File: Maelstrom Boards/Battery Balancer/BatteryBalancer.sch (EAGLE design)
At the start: 34 parts, among them P2 39-30-16, Q1 SPB80P06P, Q4 310mA/60V/1.6Ω

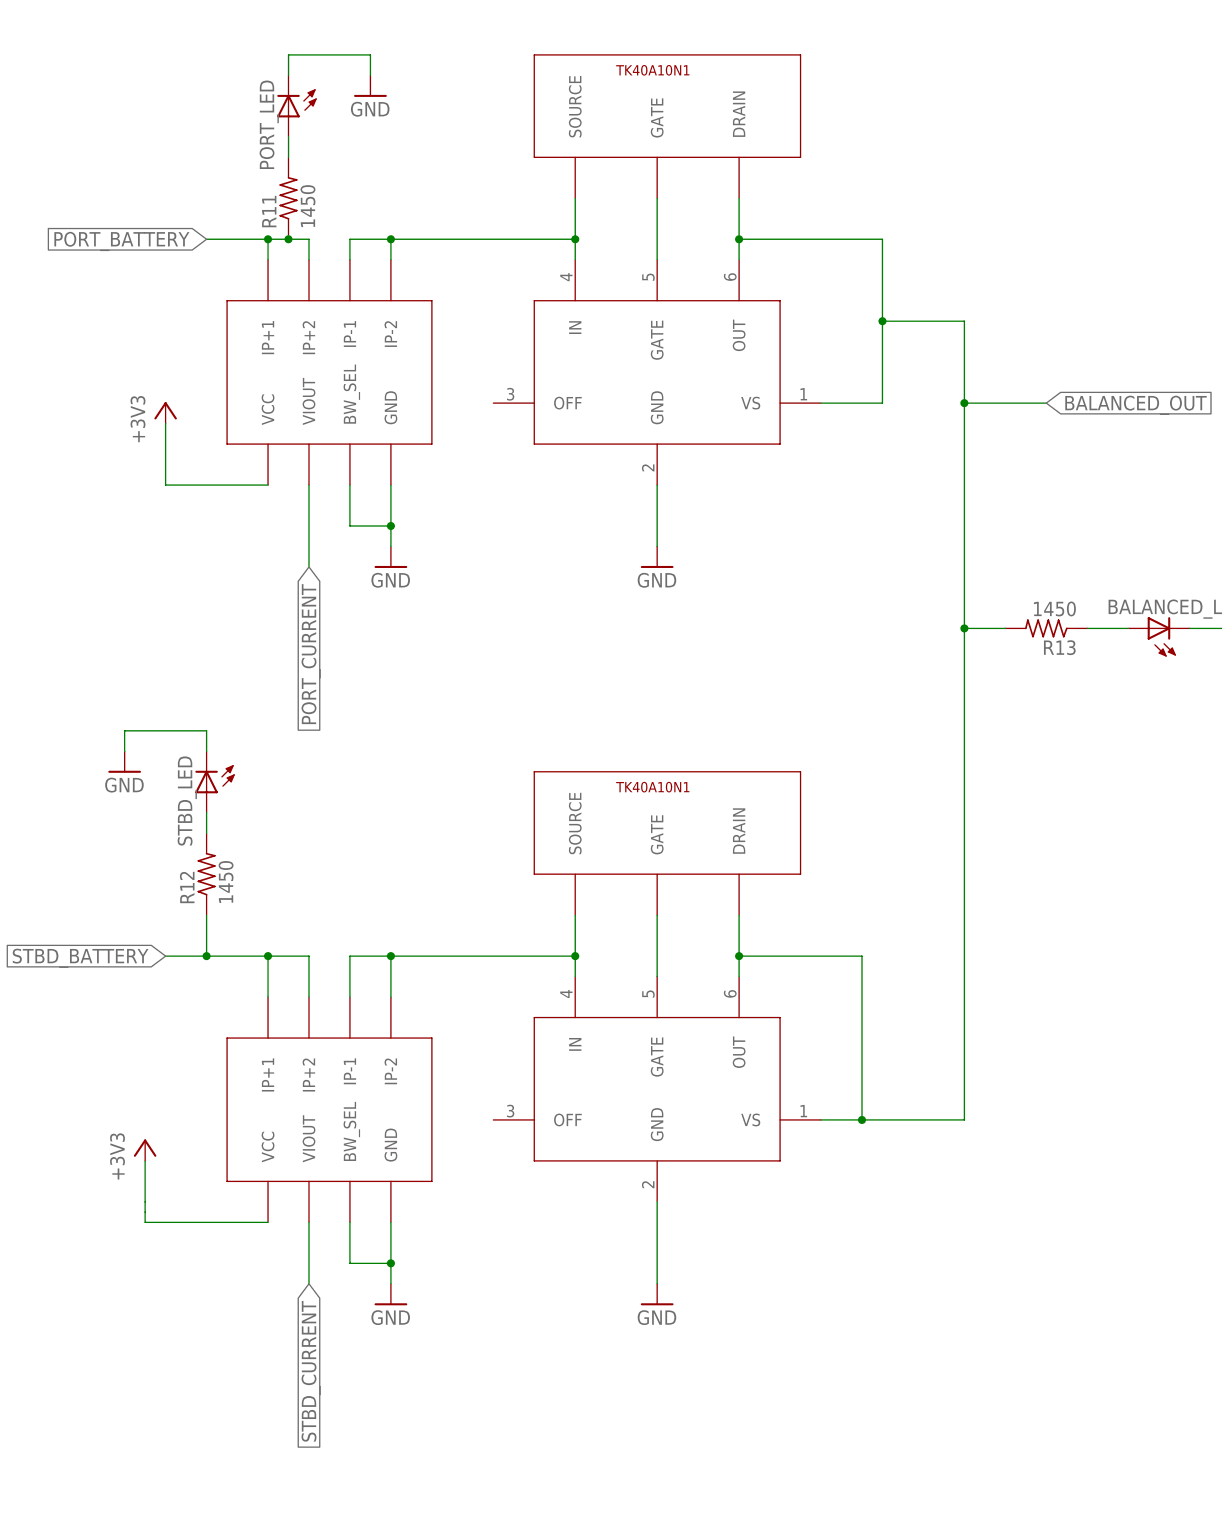
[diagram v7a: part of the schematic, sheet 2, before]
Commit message: Finishing converter and changing parts on BB
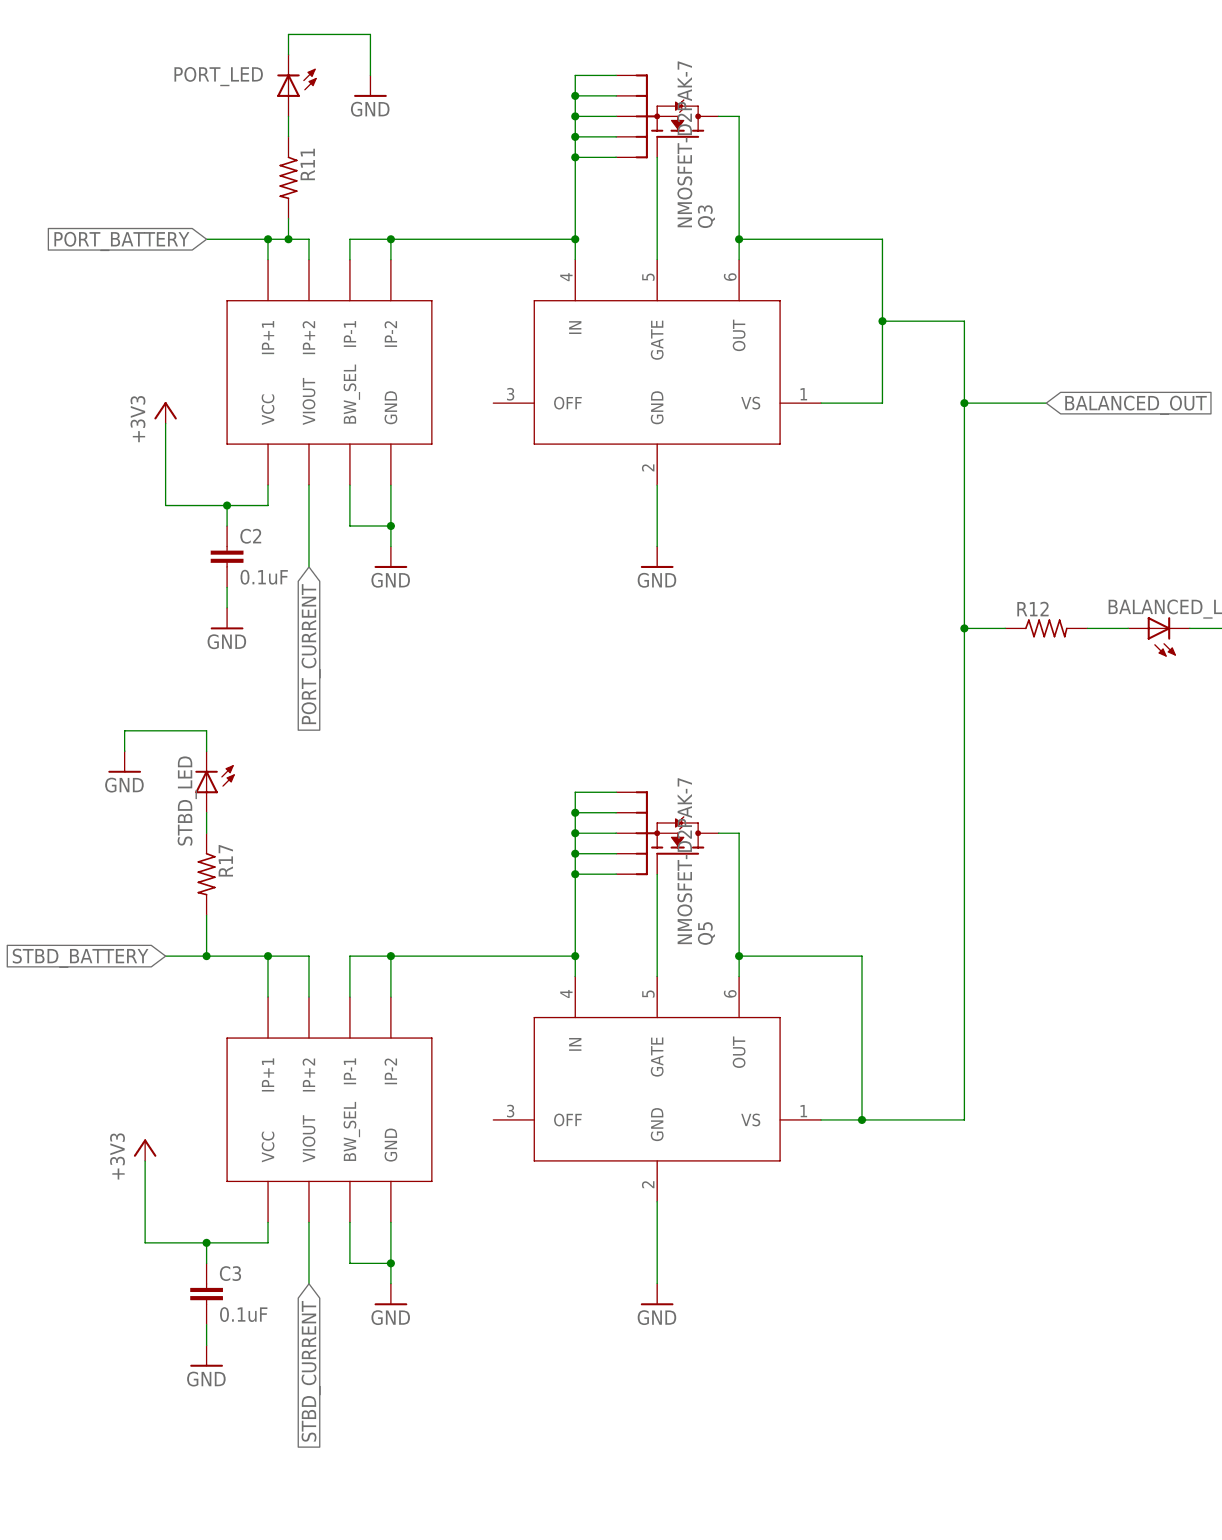
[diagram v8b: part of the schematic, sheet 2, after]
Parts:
- removed R16: 10K, rcl:R-US_R0603
- removed U$15, U$5: IXFX64N60P3TK40A10N1, TK40A10N1:IXFX64N60P3TK40A10N1
- added C2, C3: 0.1uF, rcl:C-EUC0603
- added Q2: SPB80P06P, transistor-fet:SPB80P06P
- added Q3, Q5: NMOSFET-D2PAK-7, D2PAK-7:NMOSFET-D2PAK-7
- added R17: (no value), rcl:R-US_R0603
- R11, R12, R13: value 1450 -> (none)
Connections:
- removed net GNDA: C1.2, R10.1, R3.2, R4.2, R6.1, R8.1, U$12.GND
- removed net N$14: Q1.G, R14.2, R15.1
- net +3V3: now also C2.1, C3.1, R1.1, R2.1, U$12.V+
- net BALANCED_OUT: now also Q2.S, Q3.D, Q5.D, R12.1; no longer R13.2, U$15.DRAIN, U$5.DRAIN
- net GND: now also C1.2, C2.2, C3.2, R10.1, R3.2, R4.2, R6.1, R8.1, U$12.GND
- net KILL_SWITCH: now also R13.2; no longer R16.2
- net MOTOR_POWER: now also Q2.D
- net N$1: now also Q3.S1, Q3.S2, Q3.S3, Q3.S4, Q3.S5; no longer U$15.SOURCE
- net N$11: now also R11.1; no longer R11.2
- net N$12: now also R17.1; no longer R12.2
- net N$13: now also R12.2; no longer R13.1
- net N$16: now also R13.1; no longer R16.1
- net N$2: now also Q3.G; no longer U$15.GATE
- net N$5: now also Q5.G; no longer U$5.GATE
- net N$8: now also Q1.G, Q2.G, R14.2, R15.1; no longer R1.1, R2.1, U$12.V+
- net PORT_BATTERY: now also R11.2, R9.1; no longer R11.1, R7.1
- net PORT_CURRENT: now also U$12.IN1; no longer U$12.IN0
- net SOURCE: now also Q5.S1, Q5.S2, Q5.S3, Q5.S4, Q5.S5; no longer U$5.SOURCE
- net STBD_BATTERY: now also R17.2, R7.1; no longer R12.1, R9.1
- net STBD_CURRENT: now also U$12.IN0; no longer U$12.IN1
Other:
- moved on the sheet: PORT_LED, R11, R12
